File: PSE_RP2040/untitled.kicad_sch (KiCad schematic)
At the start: 26 parts, among them J5 Barrel_Jack, U7 TPS2375-1, U8 LMR16006YQ

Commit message: correzioni schema
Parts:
- removed J5: Barrel_Jack, symbol Connector:Barrel_Jack
- added J?: (no value), symbol Connector:Screw_Terminal_01x02
- added R?: (no value), symbol Device:R
- added R?: 0R NF, symbol Device:R
- C29, C30: footprint (none) -> Capacitor_SMD:C_0603_1608Metric
- D5, D8: value D -> (none)
- D9: value D_Schottky -> (none); footprint Diode_SMD:D_SMA -> (none)
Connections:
- net GND: now also J?.2 (Pin_2), R?.2
- net poe+: now also R?.1
- net poe-: now also R?.1
- net at C29.1, C30.1, C31.1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: now also R?.2
- net at F1.1: now also J?.1 (Pin_1)
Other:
- moved on the sheet: D5
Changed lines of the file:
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@@
 (kicad_sch (version 20211123) (generator eeschema)
   (paper "A4")
+  (junction (at 95.25 74.93) (diameter 0) (color 0 0 0 0)
+  )
   (junction (at 222.25 90.17) (diameter 0) (color 0 0 0 0)
   )
@@
   (junction (at 58.42 74.93) (diameter 0) (color 0 0 0 0)
   )
+  (junction (at 45.72 116.84) (diameter 0) (color 0 0 0 0)
+  )
   (junction (at 64.77 88.9) (diameter 0) (color 0 0 0 0)
   )
@@
   (junction (at 77.47 116.84) (diameter 0) (color 0 0 0 0)
   )
+  (junction (at 109.22 74.93) (diameter 0) (color 0 0 0 0)
+  )
   (junction (at 140.97 74.93) (diameter 0) (color 0 0 0 0)
   )
@@
     (stroke (width 0) (type default) (color 0 0 0 0))
   )
+  (wire (pts (xy 45.72 132.08) (xy 45.72 116.84))
+    (stroke (width 0) (type default) (color 0 0 0 0))
+  )
   (wire (pts (xy 121.92 69.85) (xy 127 69.85))
     (stroke (width 0) (type default) (color 0 0 0 0))
@@
     (stroke (width 0) (type default) (color 0 0 0 0))
   )
-  (wire (pts (xy 88.9 74.93) (xy 106.68 74.93))
+  (wire (pts (xy 69.85 132.08) (xy 69.85 147.32))
+    (stroke (width 0) (type default) (color 0 0 0 0))
+  )
+  (wire (pts (xy 88.9 74.93) (xy 95.25 74.93))
     (stroke (width 0) (type default) (color 0 0 0 0))
   )
@@
     (stroke (width 0) (type default) (color 0 0 0 0))
   )
+  (wire (pts (xy 45.72 132.08) (xy 59.69 132.08))
+    (stroke (width 0) (type default) (color 0 0 0 0))
+  )
+  (wire (pts (xy 86.36 30.48) (xy 86.36 35.56))
+    (stroke (width 0) (type default) (color 0 0 0 0))
+  )
   (wire (pts (xy 140.97 74.93) (xy 140.97 90.17))
     (stroke (width 0) (type default) (color 0 0 0 0))
   )
-  (wire (pts (xy 82.55 27.94) (xy 92.71 27.94))
+  (wire (pts (xy 74.93 27.94) (xy 92.71 27.94))
     (stroke (width 0) (type default) (color 0 0 0 0))
   )
@@
     (stroke (width 0) (type default) (color 0 0 0 0))
   )
+  (wire (pts (xy 95.25 63.5) (xy 95.25 74.93))
+    (stroke (width 0) (type default) (color 0 0 0 0))
+  )
   (wire (pts (xy 182.88 80.01) (xy 198.12 80.01))
     (stroke (width 0) (type default) (color 0 0 0 0))
@@
     (stroke (width 0) (type default) (color 0 0 0 0))
   )
+  (wire (pts (xy 67.31 132.08) (xy 69.85 132.08))
+    (stroke (width 0) (type default) (color 0 0 0 0))
+  )
   (wire (pts (xy 81.28 116.84) (xy 81.28 101.6))
     (stroke (width 0) (type default) (color 0 0 0 0))
@@
     (stroke (width 0) (type default) (color 0 0 0 0))
   )
-  (wire (pts (xy 82.55 33.02) (xy 86.36 33.02))
-    (stroke (width 0) (type default) (color 0 0 0 0))
-  )
   (wire (pts (xy 222.25 90.17) (xy 207.01 90.17))
     (stroke (width 0) (type default) (color 0 0 0 0))
@@
     (stroke (width 0) (type default) (color 0 0 0 0))
   )
+  (wire (pts (xy 109.22 63.5) (xy 109.22 74.93))
+    (stroke (width 0) (type default) (color 0 0 0 0))
+  )
   (wire (pts (xy 121.92 69.85) (xy 121.92 74.93))
     (stroke (width 0) (type default) (color 0 0 0 0))
@@
     (stroke (width 0) (type default) (color 0 0 0 0))
   )
-  (wire (pts (xy 86.36 33.02) (xy 86.36 35.56))
-    (stroke (width 0) (type default) (color 0 0 0 0))
-  )
   (wire (pts (xy 58.42 91.44) (xy 71.12 91.44))
     (stroke (width 0) (type default) (color 0 0 0 0))
@@
     (stroke (width 0) (type default) (color 0 0 0 0))
   )
+  (wire (pts (xy 106.68 63.5) (xy 109.22 63.5))
+    (stroke (width 0) (type default) (color 0 0 0 0))
+  )
   (wire (pts (xy 234.95 80.01) (xy 234.95 81.28))
     (stroke (width 0) (type default) (color 0 0 0 0))
@@
     (stroke (width 0) (type default) (color 0 0 0 0))
   )
+  (wire (pts (xy 95.25 74.93) (xy 99.06 74.93))
+    (stroke (width 0) (type default) (color 0 0 0 0))
+  )
   (wire (pts (xy 45.72 99.06) (xy 30.48 99.06))
     (stroke (width 0) (type default) (color 0 0 0 0))
   )
+  (wire (pts (xy 99.06 63.5) (xy 95.25 63.5))
+    (stroke (width 0) (type default) (color 0 0 0 0))
+  )
   (wire (pts (xy 222.25 80.01) (xy 234.95 80.01))
     (stroke (width 0) (type default) (color 0 0 0 0))
   )
+  (wire (pts (xy 109.22 74.93) (xy 121.92 74.93))
+    (stroke (width 0) (type default) (color 0 0 0 0))
+  )
   (wire (pts (xy 128.27 74.93) (xy 140.97 74.93))
     (stroke (width 0) (type default) (color 0 0 0 0))
@@
     (stroke (width 0) (type default) (color 0 0 0 0))
   )
+  (wire (pts (xy 74.93 30.48) (xy 86.36 30.48))
+    (stroke (width 0) (type default) (color 0 0 0 0))
+  )
   (wire (pts (xy 222.25 90.17) (xy 234.95 90.17))
     (stroke (width 0) (type default) (color 0 0 0 0))
   )
-  (wire (pts (xy 114.3 74.93) (xy 121.92 74.93))
+  (wire (pts (xy 106.68 74.93) (xy 109.22 74.93))
     (stroke (width 0) (type default) (color 0 0 0 0))
   )
@@
     (pin "2")
   )
+  (symbol (lib_id "Device:R") (at 102.87 63.5 90) (unit 1)
+    (in_bom yes) (on_board yes) (fields_autoplaced)
+    (property "Reference" "R?" (id 0) (at 102.87 57.15 90))
+    (property "Value" "" (id 1) (at 102.87 59.69 90))
+    (property "Footprint" "" (id 2) (at 102.87 65.278 90)
+      (effects (font (size 1.27 1.27)) hide)
+    )
+    (property "Datasheet" "~" (id 3) (at 102.87 63.5 0)
+      (effects (font (size 1.27 1.27)) hide)
+    )
+    (pin "1")
+    (pin "2")
+  )
   (symbol (lib_id "Regulator_Switching:LMR16006YQ") (at 170.18 80.01 0) (unit 1)
     (in_bom yes) (on_board yes) (fields_autoplaced)
@@
     (pin "5")
     (pin "6")
+  )
+  (symbol (lib_id "Device:R") (at 63.5 132.08 90) (unit 1)
+    (in_bom yes) (on_board yes) (fields_autoplaced)
+    (property "Reference" "R?" (id 0) (at 63.5 125.73 90))
+    (property "Value" "0R NF" (id 1) (at 63.5 128.27 90))
+    (property "Footprint" "" (id 2) (at 63.5 133.858 90)
+      (effects (font (size 1.27 1.27)) hide)
+    )
+    (property "Datasheet" "~" (id 3) (at 63.5 132.08 0)
+      (effects (font (size 1.27 1.27)) hide)
+    )
+    (pin "1")
+    (pin "2")
   )
   (symbol (lib_id "power:+3.3V") (at 270.51 80.01 0) (unit 1)
@@
       (effects (font (size 1.27 1.27)) (justify right))
     )
-    (property "Value" "D" (id 1) (at 119.38 62.2299 90)
+    (property "Value" "" (id 1) (at 119.38 62.2299 90)
       (effects (font (size 1.27 1.27)) (justify right))
     )
@@
       (effects (font (size 1.27 1.27)) (justify right))
     )
-    (property "Value" "D_Schottky" (id 1) (at 129.54 62.5474 90)
+    (property "Value" "" (id 1) (at 129.54 62.5474 90)
       (effects (font (size 1.27 1.27)) (justify right))
     )
-    (property "Footprint" "Diode_SMD:D_SMA" (id 2) (at 127 60.96 0)
+    (property "Footprint" "" (id 2) (at 127 60.96 0)
       (effects (font (size 1.27 1.27)) hide)
     )
@@
       (effects (font (size 1.27 1.27)) (justify left))
     )
-    (property "Footprint" "" (id 2) (at 129.2352 97.79 0)
+    (property "Footprint" "Capacitor_SMD:C_0603_1608Metric" (id 2) (at 129.2352 97.79 0)
       (effects (font (size 1.27 1.27)) hide)
     )
@@
     )
     (pin "1")
+  )
+  (symbol (lib_id "Connector:Screw_Terminal_01x02") (at 69.85 27.94 0) (mirror y) (unit 1)
+    (in_bom yes) (on_board yes) (fields_autoplaced)
+    (property "Reference" "J?" (id 0) (at 69.85 21.59 0))
+    (property "Value" "" (id 1) (at 69.85 24.13 0))
+    (property "Footprint" "" (id 2) (at 69.85 27.94 0)
+      (effects (font (size 1.27 1.27)) hide)
+    )
+    (property "Datasheet" "~" (id 3) (at 69.85 27.94 0)
+      (effects (font (size 1.27 1.27)) hide)
+    )
+    (pin "1")
+    (pin "2")
   )
   (symbol (lib_id "Device:Polyfuse_Small") (at 95.25 27.94 90) (unit 1)
@@
     (pin "1")
   )
-  (symbol (lib_id "Device:D") (at 110.49 74.93 180) (unit 1)
-    (in_bom yes) (on_board yes) (fields_autoplaced)
-    (property "Reference" "D5" (id 0) (at 110.49 69.9602 0))
-    (property "Value" "D" (id 1) (at 110.49 72.4971 0))
-    (property "Footprint" "" (id 2) (at 110.49 74.93 0)
-      (effects (font (size 1.27 1.27)) hide)
-    )
-    (property "Datasheet" "~" (id 3) (at 110.49 74.93 0)
+  (symbol (lib_id "power:GND") (at 69.85 147.32 0) (unit 1)
+    (in_bom yes) (on_board yes) (fields_autoplaced)
+    (property "Reference" "#PWR?" (id 0) (at 69.85 153.67 0)
+      (effects (font (size 1.27 1.27)) hide)
+    )
+    (property "Value" "GND" (id 1) (at 69.85 151.7634 0))
+    (property "Footprint" "" (id 2) (at 69.85 147.32 0)
+      (effects (font (size 1.27 1.27)) hide)
+    )
+    (property "Datasheet" "" (id 3) (at 69.85 147.32 0)
+      (effects (font (size 1.27 1.27)) hide)
+    )
+    (pin "1")
+  )
+  (symbol (lib_id "Device:D") (at 102.87 74.93 180) (unit 1)
+    (in_bom yes) (on_board yes) (fields_autoplaced)
+    (property "Reference" "D5" (id 0) (at 102.87 68.58 0))
+    (property "Value" "" (id 1) (at 102.87 71.12 0))
+    (property "Footprint" "" (id 2) (at 102.87 74.93 0)
+      (effects (font (size 1.27 1.27)) hide)
+    )
+    (property "Datasheet" "~" (id 3) (at 102.87 74.93 0)
       (effects (font (size 1.27 1.27)) hide)
     )
@@
     (pin "1")
   )
-  (symbol (lib_id "Connector:Barrel_Jack") (at 74.93 30.48 0) (unit 1)
-    (in_bom yes) (on_board yes) (fields_autoplaced)
-    (property "Reference" "J5" (id 0) (at 74.93 21.59 0))
-    (property "Value" "Barrel_Jack" (id 1) (at 74.93 24.13 0))
-    (property "Footprint" "" (id 2) (at 76.2 31.496 0)
-      (effects (font (size 1.27 1.27)) hide)
-    )
-    (property "Datasheet" "~" (id 3) (at 76.2 31.496 0)
-      (effects (font (size 1.27 1.27)) hide)
-    )
-    (pin "1")
-    (pin "2")
-  )
   (symbol (lib_id "Device:C") (at 140.97 93.98 0) (unit 1)
     (in_bom yes) (on_board yes) (fields_autoplaced)
@@
       (effects (font (size 1.27 1.27)) (justify left))
     )
-    (property "Footprint" "" (id 2) (at 141.9352 97.79 0)
-      (effects (font (size 1.27 1.27)) hide)
-    )
+    (property "Footprint" "Capacitor_SMD:C_0603_1608Metric" (id 2) (at 141.9352 97.79 0)
+      (effects (font (size 1.27 1.27)) hide)
+    )

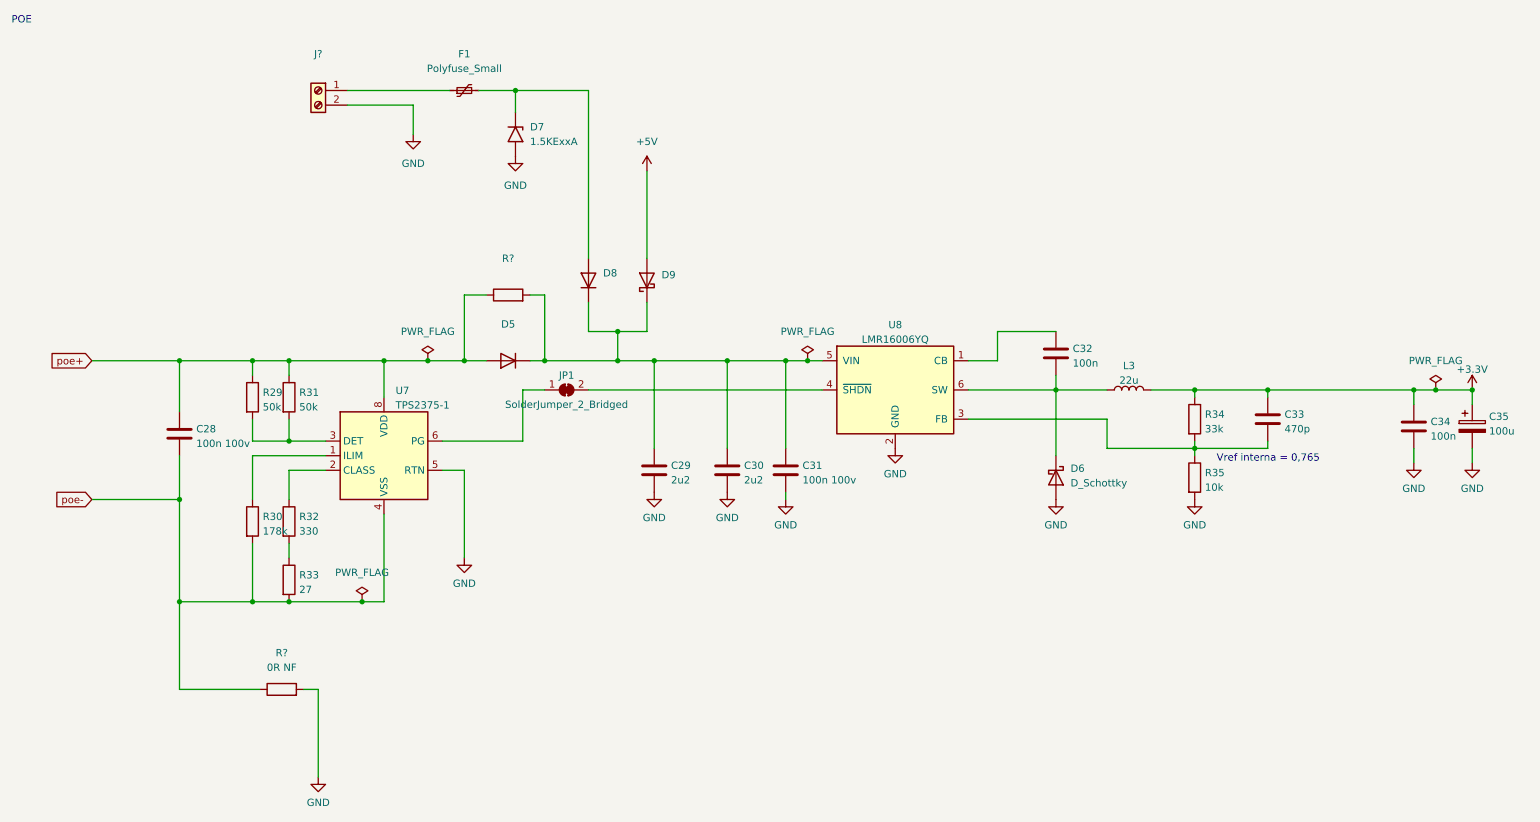
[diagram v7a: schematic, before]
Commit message: footprint, assegnamento
etichette (label)
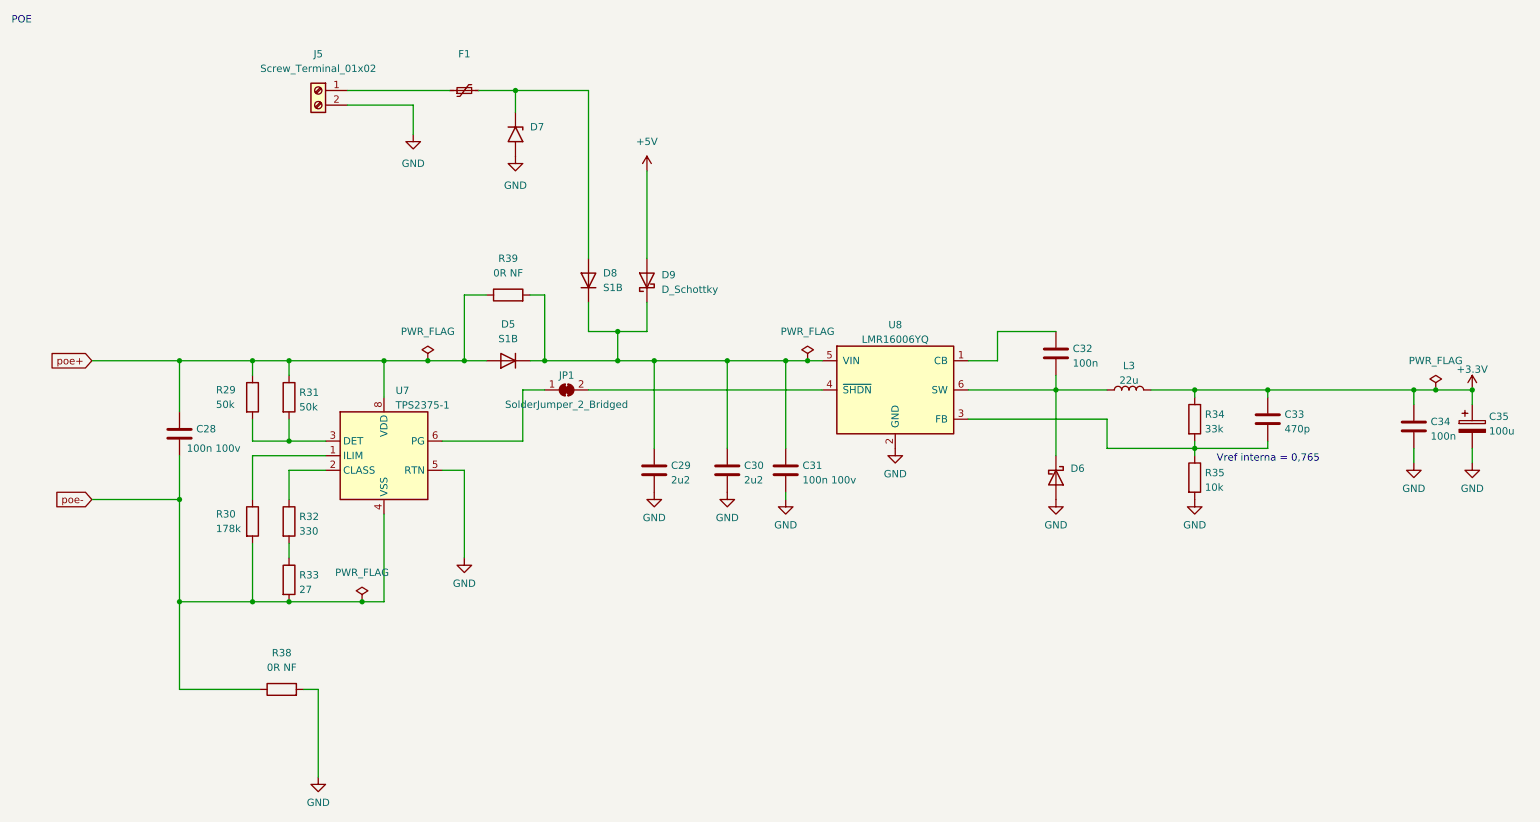
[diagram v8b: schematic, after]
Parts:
- D5, D8: value (none) -> S1B; footprint (none) -> Diode_SMD:D_SMA
- D6: value D_Schottky -> (none); footprint Diode_SMD:D_SMA -> (none)
- D7: value 1.5KExxA -> (none); footprint Diode_THT:D_DO-201AE_P15.24mm_Horizontal -> (none)
- D9: value (none) -> D_Schottky; footprint (none) -> Diode_SMD:D_SMA
- F1: value Polyfuse_Small -> (none)
- J5: renamed from J?; value (none) -> Screw_Terminal_01x02; footprint (none) -> TerminalBlock_Phoenix:TerminalBlock_Phoenix_MKDS-1,5-2-5.08_1x02_P5.08mm_Horizontal
- R39: renamed from R?; value (none) -> 0R NF
- gave numbers to parts that had none: 1
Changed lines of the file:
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@@
   (symbol (lib_id "Device:R") (at 102.87 63.5 90) (unit 1)
     (in_bom yes) (on_board yes) (fields_autoplaced)
-    (property "Reference" "R?" (id 0) (at 102.87 57.15 90))
-    (property "Value" "" (id 1) (at 102.87 59.69 90))
+    (property "Reference" "R39" (id 0) (at 102.87 57.15 90))
+    (property "Value" "0R NF" (id 1) (at 102.87 59.69 90))
     (property "Footprint" "" (id 2) (at 102.87 65.278 90)
       (effects (font (size 1.27 1.27)) hide)
@@
   (symbol (lib_id "Device:R") (at 63.5 132.08 90) (unit 1)
     (in_bom yes) (on_board yes) (fields_autoplaced)
-    (property "Reference" "R?" (id 0) (at 63.5 125.73 90))
+    (property "Reference" "R38" (id 0) (at 63.5 125.73 90))
     (property "Value" "0R NF" (id 1) (at 63.5 128.27 90))
     (property "Footprint" "" (id 2) (at 63.5 133.858 90)
@@
       (effects (font (size 1.27 1.27)) (justify right))
     )
-    (property "Value" "" (id 1) (at 119.38 62.2299 90)
+    (property "Value" "S1B" (id 1) (at 119.38 62.2299 90)
       (effects (font (size 1.27 1.27)) (justify right))
     )
-    (property "Footprint" "" (id 2) (at 116.84 60.96 0)
+    (property "Footprint" "Diode_SMD:D_SMA" (id 2) (at 116.84 60.96 0)
       (effects (font (size 1.27 1.27)) hide)
     )
@@
   )
   (symbol (lib_id "Device:R") (at 58.42 81.28 0) (unit 1)
-    (in_bom yes) (on_board yes) (fields_autoplaced)
-    (property "Reference" "R29" (id 0) (at 60.198 80.4453 0)
-      (effects (font (size 1.27 1.27)) (justify left))
-    )
-    (property "Value" "50k" (id 1) (at 60.198 82.9822 0)
+    (in_bom yes) (on_board yes)
+    (property "Reference" "R29" (id 0) (at 52.07 80.0131 0)
+      (effects (font (size 1.27 1.27)) (justify left))
+    )
+    (property "Value" "50k" (id 1) (at 52.07 82.55 0)
       (effects (font (size 1.27 1.27)) (justify left))
     )
@@
       (effects (font (size 1.27 1.27)) (justify right))
     )
-    (property "Value" "" (id 1) (at 129.54 62.5474 90)
+    (property "Value" "D_Schottky" (id 1) (at 129.54 62.5474 90)
       (effects (font (size 1.27 1.27)) (justify right))
     )
-    (property "Footprint" "" (id 2) (at 127 60.96 0)
+    (property "Footprint" "Diode_SMD:D_SMA" (id 2) (at 127 60.96 0)
       (effects (font (size 1.27 1.27)) hide)
     )
@@
       (effects (font (size 1.27 1.27)) (justify left))
     )
-    (property "Value" "D_Schottky" (id 1) (at 200.66 96.2024 90)
-      (effects (font (size 1.27 1.27)) (justify left))
-    )
-    (property "Footprint" "Diode_SMD:D_SMA" (id 2) (at 198.12 95.25 0)
+    (property "Value" "" (id 1) (at 200.66 96.2024 90)
+      (effects (font (size 1.27 1.27)) (justify left))
+    )
+    (property "Footprint" "" (id 2) (at 198.12 95.25 0)
       (effects (font (size 1.27 1.27)) hide)
     )
@@
   (symbol (lib_id "Connector:Screw_Terminal_01x02") (at 69.85 27.94 0) (mirror y) (unit 1)
     (in_bom yes) (on_board yes) (fields_autoplaced)
-    (property "Reference" "J?" (id 0) (at 69.85 21.59 0))
-    (property "Value" "" (id 1) (at 69.85 24.13 0))
-    (property "Footprint" "" (id 2) (at 69.85 27.94 0)
+    (property "Reference" "J5" (id 0) (at 69.85 21.59 0))
+    (property "Value" "Screw_Terminal_01x02" (id 1) (at 69.85 24.13 0))
+    (property "Footprint" "TerminalBlock_Phoenix:TerminalBlock_Phoenix_MKDS-1,5-2-5.08_1x02_P5.08mm_Horizontal" (id 2) (at 69.85 27.94 0)
       (effects (font (size 1.27 1.27)) hide)
     )
@@
     (in_bom yes) (on_board yes) (fields_autoplaced)
     (property "Reference" "F1" (id 0) (at 95.25 21.59 90))
-    (property "Value" "Polyfuse_Small" (id 1) (at 95.25 24.13 90))
+    (property "Value" "" (id 1) (at 95.25 24.13 90))
     (property "Footprint" "" (id 2) (at 100.33 26.67 0)
       (effects (font (size 1.27 1.27)) (justify left) hide)
@@
       (effects (font (size 1.27 1.27)) (justify left))
     )
-    (property "Value" "1.5KExxA" (id 1) (at 106.68 36.8299 90)
-      (effects (font (size 1.27 1.27)) (justify left))
-    )
-    (property "Footprint" "Diode_THT:D_DO-201AE_P15.24mm_Horizontal" (id 2) (at 99.06 35.56 0)
+    (property "Value" "" (id 1) (at 106.68 36.8299 90)
+      (effects (font (size 1.27 1.27)) (justify left))
+    )
+    (property "Footprint" "" (id 2) (at 99.06 35.56 0)
       (effects (font (size 1.27 1.27)) hide)
     )
@@
   (symbol (lib_id "power:GND") (at 69.85 147.32 0) (unit 1)
     (in_bom yes) (on_board yes) (fields_autoplaced)
-    (property "Reference" "#PWR?" (id 0) (at 69.85 153.67 0)
+    (property "Reference" "#PWR04" (id 0) (at 69.85 153.67 0)
       (effects (font (size 1.27 1.27)) hide)
     )
@@
     (in_bom yes) (on_board yes) (fields_autoplaced)
     (property "Reference" "D5" (id 0) (at 102.87 68.58 0))
-    (property "Value" "" (id 1) (at 102.87 71.12 0))
-    (property "Footprint" "" (id 2) (at 102.87 74.93 0)
+    (property "Value" "S1B" (id 1) (at 102.87 71.12 0))
+    (property "Footprint" "Diode_SMD:D_SMA" (id 2) (at 102.87 74.93 0)
       (effects (font (size 1.27 1.27)) hide)
     )
@@
   )
   (symbol (lib_id "Device:C") (at 45.72 87.63 0) (unit 1)
-    (in_bom yes) (on_board yes) (fields_autoplaced)
+    (in_bom yes) (on_board yes)
     (property "Reference" "C28" (id 0) (at 48.641 86.7953 0)
       (effects (font (size 1.27 1.27)) (justify left))
     )
-    (property "Value" "100n 100v" (id 1) (at 48.641 89.3322 0)
+    (property "Value" "100n 100v" (id 1) (at 46.99 90.17 0)
       (effects (font (size 1.27 1.27)) (justify left))
     )
@@
   )
   (symbol (lib_id "Device:R") (at 58.42 102.87 0) (unit 1)
-    (in_bom yes) (on_board yes) (fields_autoplaced)
-    (property "Reference" "R30" (id 0) (at 60.198 102.0353 0)
-      (effects (font (size 1.27 1.27)) (justify left))
-    )
-    (property "Value" "178k" (id 1) (at 60.198 104.5722 0)
-      (effects (font (size 1.27 1.27)) (justify left))
-    )
+    (in_bom yes) (on_board yes)
+    (property "Reference" "R30" (id 0) (at 52.07 101.6 0)
+      (effects (font (size 1.27 1.27)) (justify left))
+    )
+    (property "Value" "178k" (id 1) (at 52.07 104.1369 0)
+      (effects (font (size 1.27 1.27)) (justify left))
+    )
